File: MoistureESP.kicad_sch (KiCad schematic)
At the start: 4 parts, among them J2 Conn_MoisturePCB, J3 Conn_DS18B20, SW1 147873-1

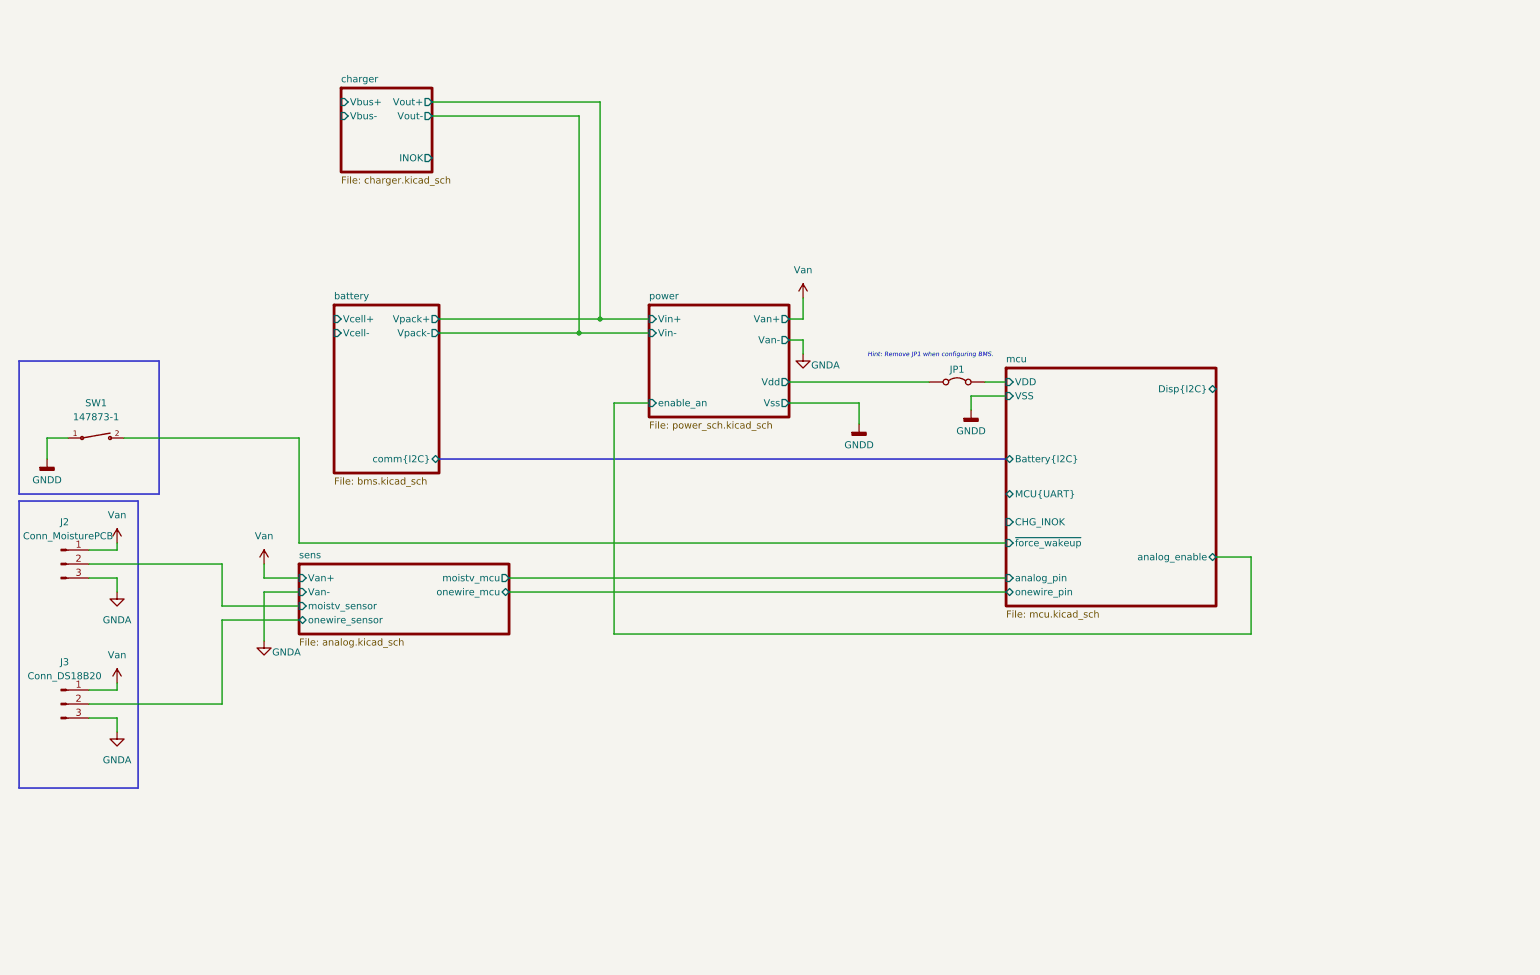
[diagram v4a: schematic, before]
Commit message: Add charger, battery cell.
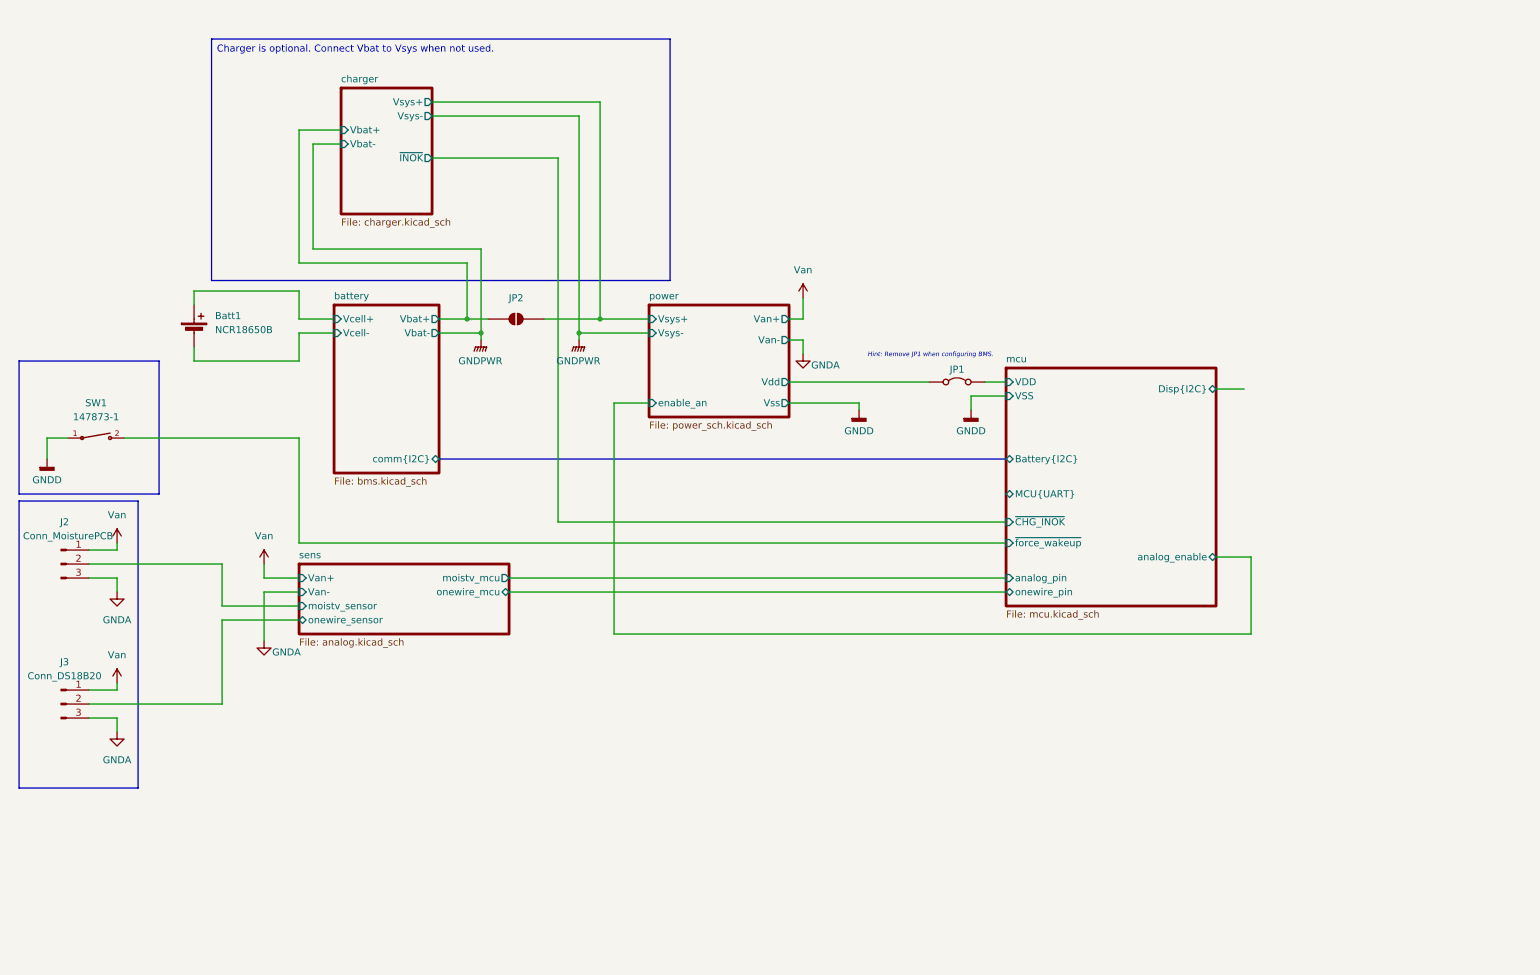
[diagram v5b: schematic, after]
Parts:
- added Batt1: NCR18650B, custom:NCR18650, symbol custom:Battery_Cell
- added JP2: SolderJumper_2_Open, Jumper:SolderJumper-2_P1.3mm_Open_TrianglePad1.0x1.5mm, symbol Jumper:SolderJumper_2_Open
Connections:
- net battery/Vcell+: now also Batt1.1 (+)
- net battery/Vcell-: now also Batt1.2 (-)
- new net battery/Vbat+: JP2.1 (A)
- new net charger/Vsys+: JP2.2 (B)
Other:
- sheet battery ports: added Vbat+, Vbat-; removed Vpack+, Vpack-
- sheet charger ports: added Vbat+, Vbat-, Vsys+, Vsys-, ~{INOK}; removed INOK, Vbus+, Vbus-, Vout+, Vout-
- sheet mcu ports: added ~{CHG_INOK}; removed CHG_INOK
- sheet power ports: added Vsys+, Vsys-; removed Vin+, Vin-

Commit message: Add console port.
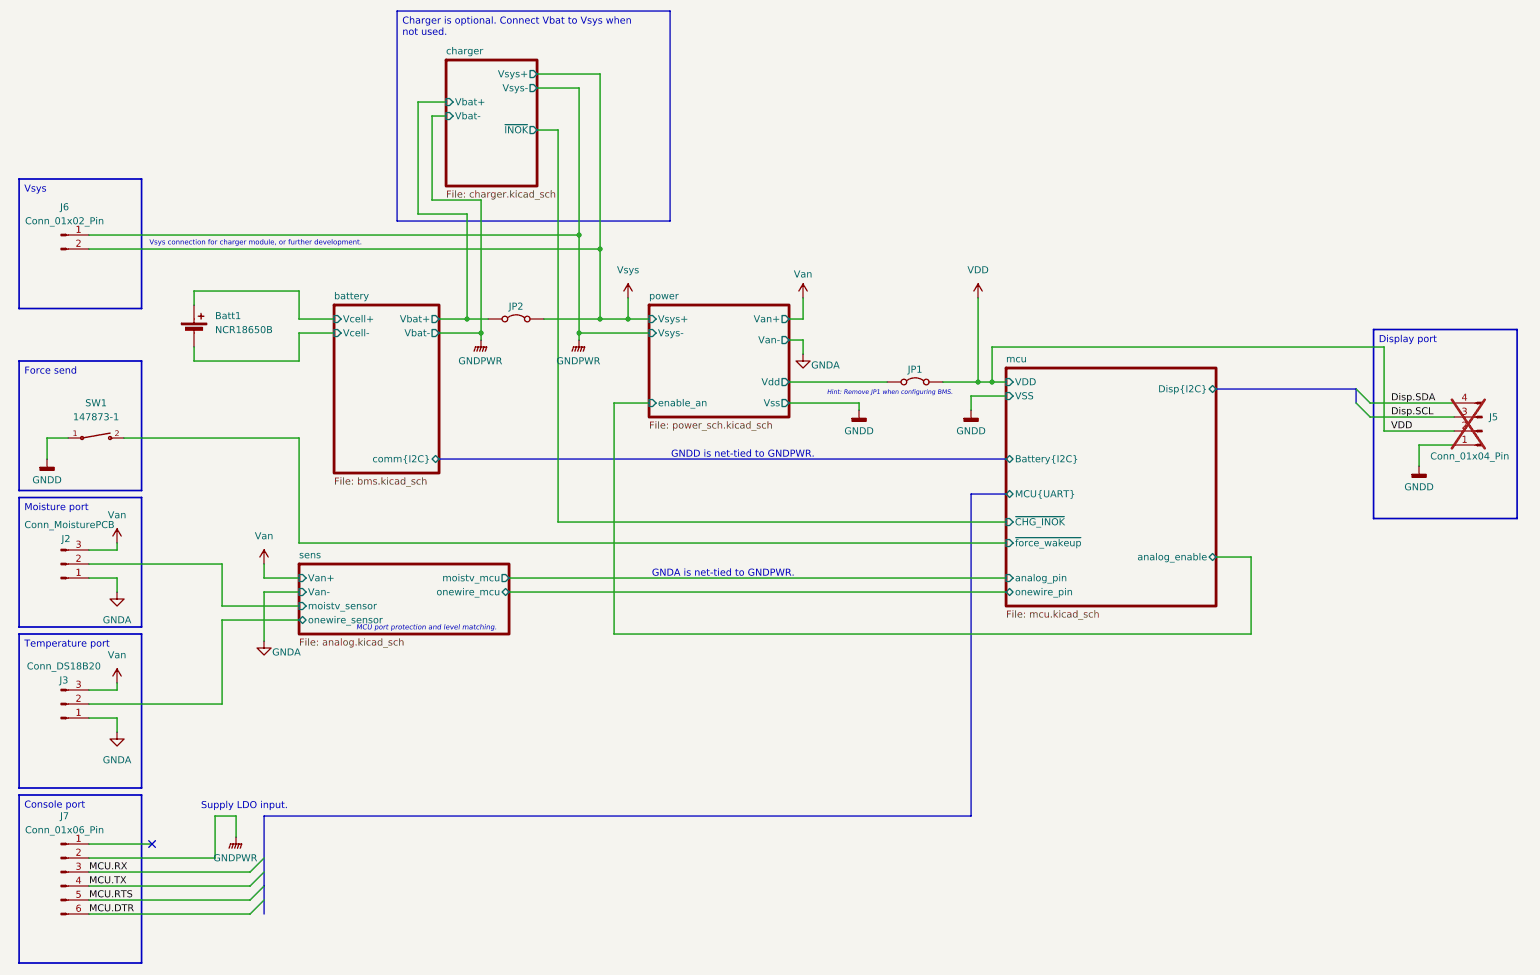
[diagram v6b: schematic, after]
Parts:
- removed JP2: SolderJumper_2_Open, Jumper:SolderJumper-2_P1.3mm_Open_TrianglePad1.0x1.5mm, symbol Jumper:SolderJumper_2_Open
- added J5: Conn_01x04_Pin, symbol Connector:Conn_01x04_Pin
- added J6: Conn_01x02_Pin, symbol Connector:Conn_01x02_Pin
- added J7: Conn_01x06_Pin, symbol Connector:Conn_01x06_Pin
- added JP2: Jumper_2_Bridged, Connector_PinHeader_2.54mm:PinHeader_1x02_P2.54mm_Horizontal, symbol Jumper:Jumper_2_Bridged
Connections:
- net GNDA: now also J2.1 (Pin_1), J3.1 (Pin_1); no longer J2.3 (Pin_3), J3.3 (Pin_3)
- net GNDD: now also J5.1 (Pin_1)
- net GNDPWR: now also J6.1 (Pin_1), J7.2 (Pin_2)
- net Van: now also J2.3 (Pin_3), J3.3 (Pin_3); no longer J2.1 (Pin_1), J3.1 (Pin_1)
- net battery/Vbat+: now also JP2.1 (A)
- net mcu/VDD renamed VDD
- net VDD: now also J5.2 (Pin_2)
- new net Disp.SCL: J5.3 (Pin_3)
- new net Disp.SDA: J5.4 (Pin_4)
- new net MCU.DTR: J7.6 (Pin_6)
- new net MCU.RTS: J7.5 (Pin_5)
- new net MCU.RX: J7.3 (Pin_3)
- new net MCU.TX: J7.4 (Pin_4)
- new net Vsys: J6.2 (Pin_2), JP2.2 (B)
- no-connect marks 0 -> 1
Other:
- note added: "GNDA is net-tied to GNDPWR."
- note added: "GNDD is net-tied to GNDPWR."
- note added: "MCU port protection and level matching."
- note added: "Supply LDO input."
- note added: "Vsys connection for charger module, or further development."
- moved on the sheet: JP1

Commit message: Fix issues
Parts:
- added D6: BZT52H-B18, Diode_SMD:D_SOD-123F, symbol Diode:BZT52Bxx
- added J1: Conn_01x03_Pin, Connector_PinHeader_2.54mm:PinHeader_1x03_P2.54mm_Horizontal, symbol Connector:Conn_01x03_Pin
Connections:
- net GNDPWR: now also D6.2 (A), J1.1 (Pin_1)
- net Vsys: now also D6.1 (K)
- new net Battery.SCL: J1.3 (Pin_3)
- new net Battery.SDA: J1.2 (Pin_2)
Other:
- moved on the sheet: SW1

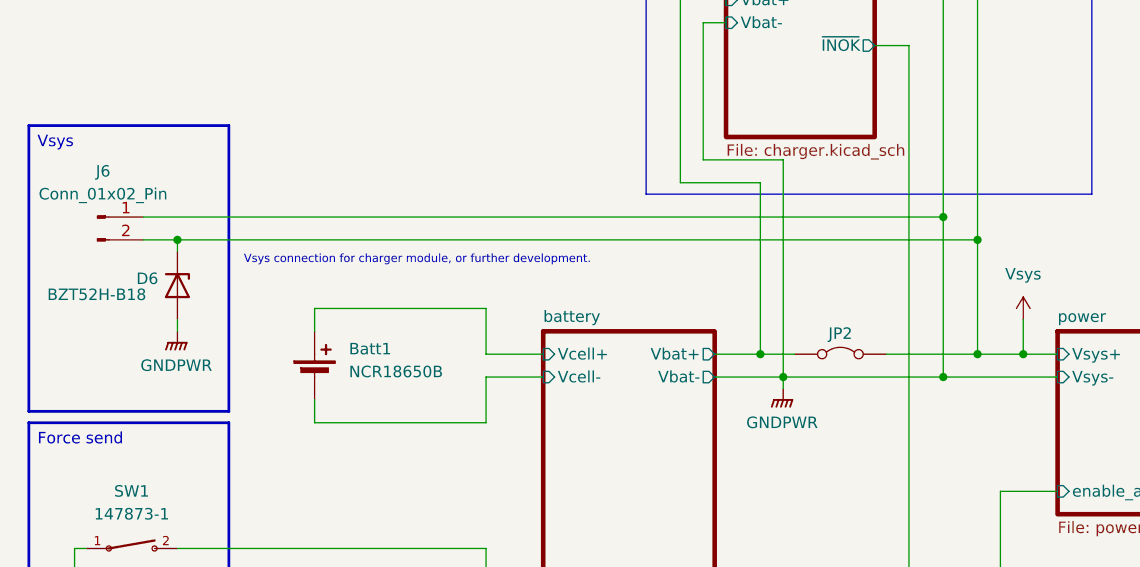
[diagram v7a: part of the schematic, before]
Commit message: Fix issues from Issue#1
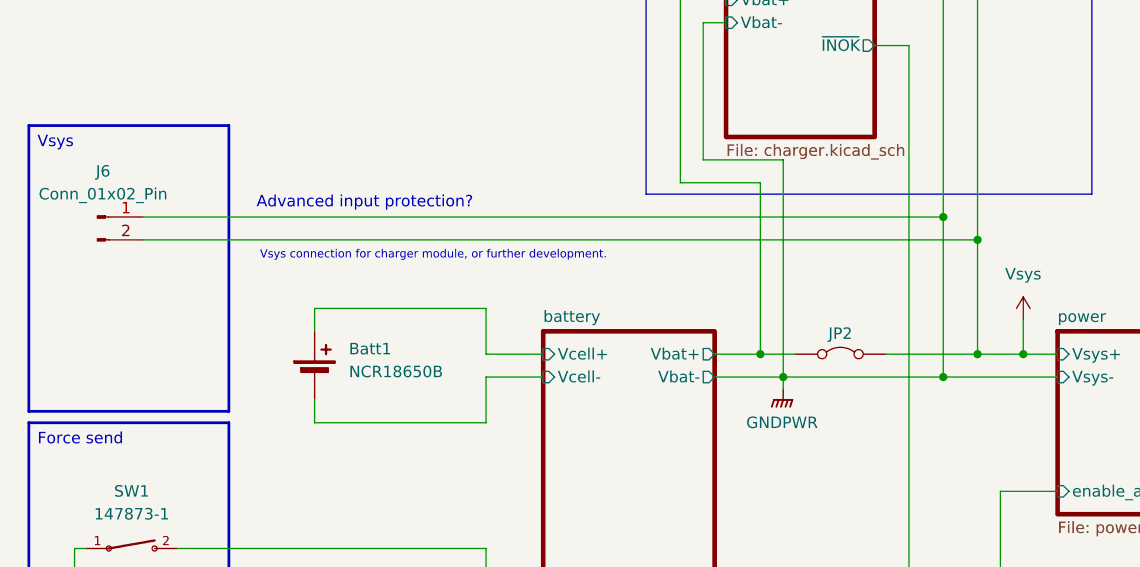
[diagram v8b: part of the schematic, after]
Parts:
- removed D6: BZT52H-B18, Diode_SMD:D_SOD-123F, symbol Diode:BZT52Bxx
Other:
- note added: "Advanced input protection?"
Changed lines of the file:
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@@
 	(text "Vsys connection for charger module, or further development."
 		(exclude_from_sim no)
-		(at 55.88 59.436 0)
+		(at 57.658 58.928 0)
 		(effects
 			(font
@@
 		)
 	)
+	(text "Advanced input protection?"
+		(exclude_from_sim no)
+		(at 50.038 53.086 0)
+		(effects
+			(font
+				(size 1.27 1.27)
+			)
+		)
+	)
 	(text_box "Vsys"
 		(exclude_from_sim no)
@@
 	)
 	(junction
-		(at 29.21 57.15)
-		(diameter 0)
-		(color 0 0 0 0)
-	)
-	(junction
 		(at 186.69 81.28)
 		(diameter 0)
@@
 	(wire
 		(pts
-			(xy 29.21 57.15) (xy 29.21 58.42)
-		)
-		(stroke
-			(width 0)
-			(type default)
-		)
-	)
-	(wire
-		(pts
 			(xy 44.45 77.47) (xy 44.45 74.93)
 		)
@@
 	(wire
 		(pts
-			(xy 29.21 66.04) (xy 29.21 67.31)
-		)
-		(stroke
-			(width 0)
-			(type default)
-		)
-	)
-	(wire
-		(pts
 			(xy 87.63 33.02) (xy 87.63 48.26)
 		)
@@
 	(wire
 		(pts
-			(xy 25.4 57.15) (xy 29.21 57.15)
+			(xy 25.4 57.15) (xy 118.11 57.15)
 		)
 		(stroke
@@
 		(pts
 			(xy 54.61 170.18) (xy 25.4 170.18)
-		)
-		(stroke
-			(width 0)
-			(type default)
-		)
-	)
-	(wire
-		(pts
-			(xy 29.21 57.15) (xy 118.11 57.15)
 		)
 		(stroke
@@
 	)
 	(symbol
-		(lib_id "Diode:BZT52Bxx")
-		(at 29.21 62.23 270)
-		(unit 1)
-		(body_style 1)
-		(exclude_from_sim no)
-		(in_bom yes)
-		(on_board yes)
-		(in_pos_files yes)
-		(dnp no)
-		(property "Reference" "D6"
-			(at 24.638 61.468 90)
-			(show_name no)
-			(do_not_autoplace no)
-			(effects
-				(font
-					(size 1.27 1.27)
-				)
-				(justify left)
-			)
-		)
-		(property "Value" "BZT52H-B18"
-			(at 14.732 63.246 90)
-			(show_name no)
-			(do_not_autoplace no)
-			(effects
-				(font
-					(size 1.27 1.27)
-				)
-				(justify left)
-			)
-		)
-		(property "Footprint" "Diode_SMD:D_SOD-123F"
-			(at 24.765 62.23 0)
-			(hide yes)
-			(show_name no)
-			(do_not_autoplace no)
-			(effects
-				(font
-					(size 1.27 1.27)
-				)
-			)
-		)
-		(property "Datasheet" "https://diotec.com/tl_files/diotec/files/pdf/datasheets/bzt52b2v4.pdf"
-			(at 29.21 62.23 0)
-			(hide yes)
-			(show_name no)
-			(do_not_autoplace no)
-			(effects
-				(font
-					(size 1.27 1.27)
-				)
-			)
-		)
-		(property "Description" "500mW Zener Diode, SOD-123F"
-			(at 29.21 62.23 0)
-			(hide yes)
-			(show_name no)
-			(do_not_autoplace no)
-			(effects
-				(font
-					(size 1.27 1.27)
-				)
-			)
-		)
-		(pin "1"
-		)
-		(pin "2"
-		)
-		(instances
-			(project "MoistureESP"
-				(path "/f2b9f638-139e-46ec-aa60-77c4af989196"
-					(reference "D6")
-					(unit 1)
-				)
-			)
-		)
-	)
-	(symbol
 		(lib_id "power:VAA")
 		(at 154.94 66.04 0)
@@
 					(unit 1)
 				)
-			)
-		)
-	)
-	(symbol
-		(lib_id "power:GNDPWR")
-		(at 29.21 67.31 0)
-		(unit 1)
-		(body_style 1)
-		(exclude_from_sim no)
-		(in_bom yes)
-		(on_board yes)
-		(in_pos_files yes)
-		(dnp no)
-		(fields_autoplaced yes)
-		(property "Reference" "#PWR066"
-			(at 29.21 72.39 0)
-			(hide yes)
-			(show_name no)
-			(do_not_autoplace no)
-			(effects
-				(font
-					(size 1.27 1.27)
-				)
-			)
-		)
-		(property "Value" "GNDPWR"
-			(at 29.083 71.12 0)
-			(show_name no)
-			(do_not_autoplace no)
-			(effects
-				(font
-					(size 1.27 1.27)
-				)
-			)
-		)
-		(property "Footprint" ""
-			(at 29.21 68.58 0)
-			(hide yes)
-			(show_name no)
-			(do_not_autoplace no)
-			(effects
-				(font
-					(size 1.27 1.27)
-				)
-			)
-		)
-		(property "Datasheet" ""
-			(at 29.21 68.58 0)
-			(hide yes)
-			(show_name no)
-			(do_not_autoplace no)
-			(effects
-				(font
-					(size 1.27 1.27)
-				)
-			)
-		)
-		(property "Description" "Power symbol creates a global label with name \"GNDPWR\" , global ground"
-			(at 29.21 67.31 0)
-			(hide yes)
-			(show_name no)
-			(do_not_autoplace no)
-			(effects
-				(font
-					(size 1.27 1.27)
-				)
-			)
-		)
-		(pin "1"
-		)
-		(instances
-			(project "MoistureESP"
-				(path "/f2b9f638-139e-46ec-aa60-77c4af989196"
-					(reference "#PWR066")
-					(unit 1)
-				)
